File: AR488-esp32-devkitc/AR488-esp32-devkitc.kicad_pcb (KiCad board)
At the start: 2 copper layers, 63.5 x 50 mm, 7 parts, among them J2 Conn_02x12_Odd_Even, U2 ESP32-DevKitC

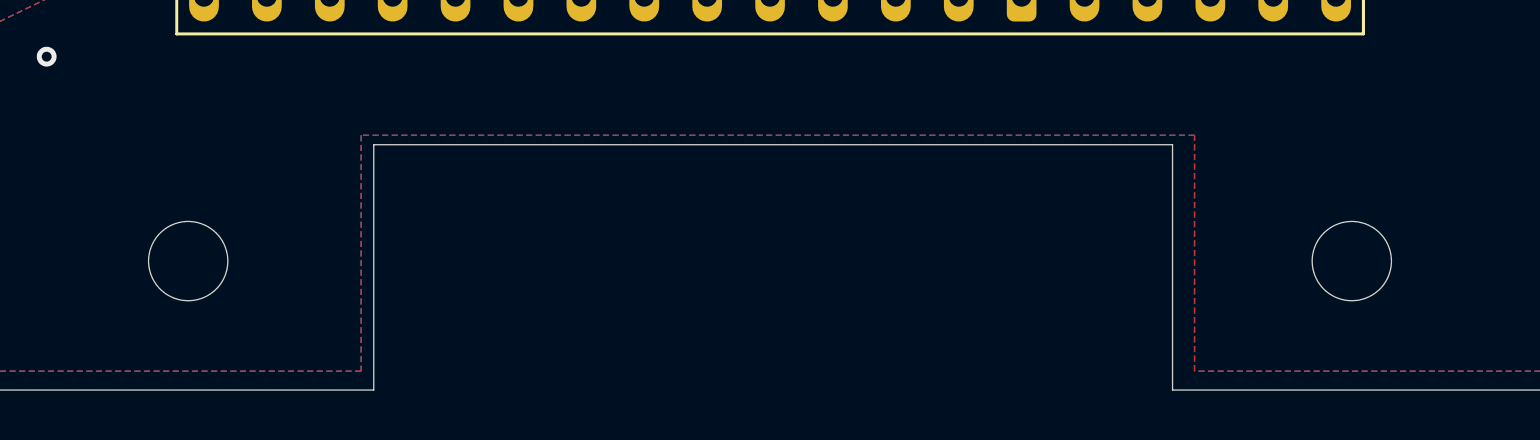
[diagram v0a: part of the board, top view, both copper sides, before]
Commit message: Several minor fixes and adjustments in PCBs
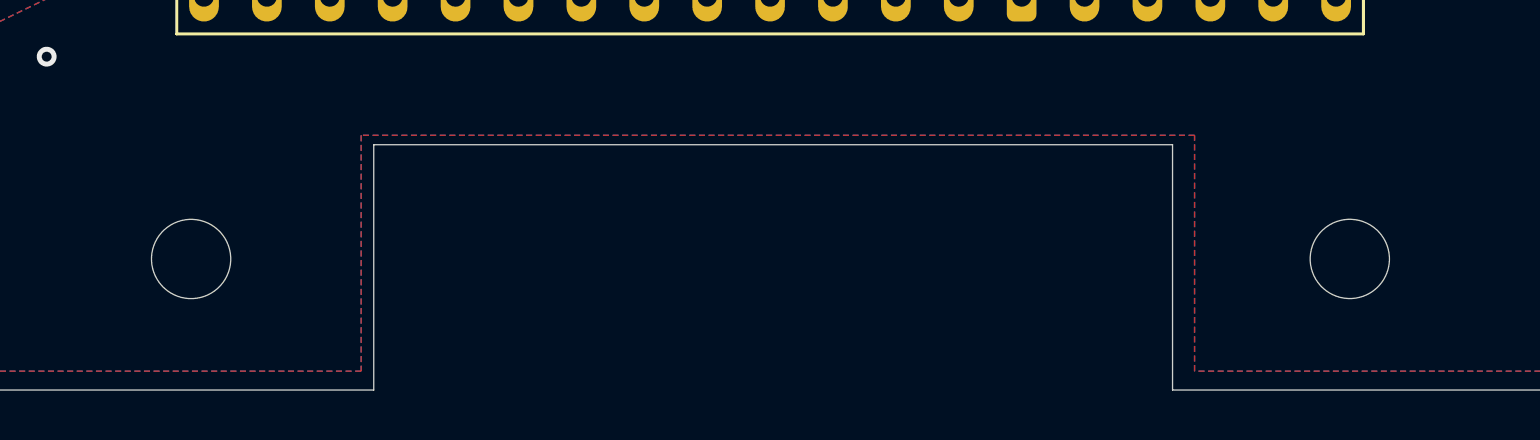
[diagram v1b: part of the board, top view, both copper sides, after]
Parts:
- moved REF** 0.15 mm to (71.4, 108.2)
- moved REF** 0.12 mm to (118.2, 108.2)
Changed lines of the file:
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@@
   (general
     (thickness 1.6)
-    (drawings 107)
+    (drawings 108)
     (tracks 100)
     (zones 0)
@@
       (outputformat 1)
       (mirror false)
-      (drillshape 1)
+      (drillshape 0)
       (scaleselection 1)
       (outputdirectory ""))
@@
   )
   (module MountingHole:MountingHole_3.2mm_M3_ISO7380 (layer F.Cu)
-    (at 118.245 108.325)
+    (at 118.164336 108.237955)
     (descr "Mounting Hole 3.2mm, no annular, M3, ISO7380")
     (tags "mounting hole 3.2mm no annular m3 iso7380")
@@
   )
   (module MountingHole:MountingHole_3.2mm_M3_ISO7380 (layer F.Cu)
-    (at 71.255 108.325)
+    (at 71.372767 108.240114)
     (descr "Mounting Hole 3.2mm, no annular, M3, ISO7380")
     (tags "mounting hole 3.2mm no annular m3 iso7380")
@@
     )
   )
+  (dimension 4.445 (width 0.15) (layer Dwgs.User)
+    (gr_text "4.445 mm" (at 65.2225 58.13) (layer Dwgs.User)
+      (effects (font (size 1 1) (thickness 0.15)))
+    )
+    (feature1 (pts (xy 63 67.685) (xy 63 58.843579)))
+    (feature2 (pts (xy 67.445 67.685) (xy 67.445 58.843579)))
+    (crossbar (pts (xy 67.445 59.43) (xy 63 59.43)))
+    (arrow1a (pts (xy 63 59.43) (xy 64.126504 58.843579)))
+    (arrow1b (pts (xy 63 59.43) (xy 64.126504 60.016421)))
+    (arrow2a (pts (xy 67.445 59.43) (xy 66.318496 58.843579)))
+    (arrow2b (pts (xy 67.445 59.43) (xy 66.318496 60.016421)))
+  )
   (gr_text http://whatever.sdfa3.org/gpib (at 98.56 75.305) (layer B.SilkS)

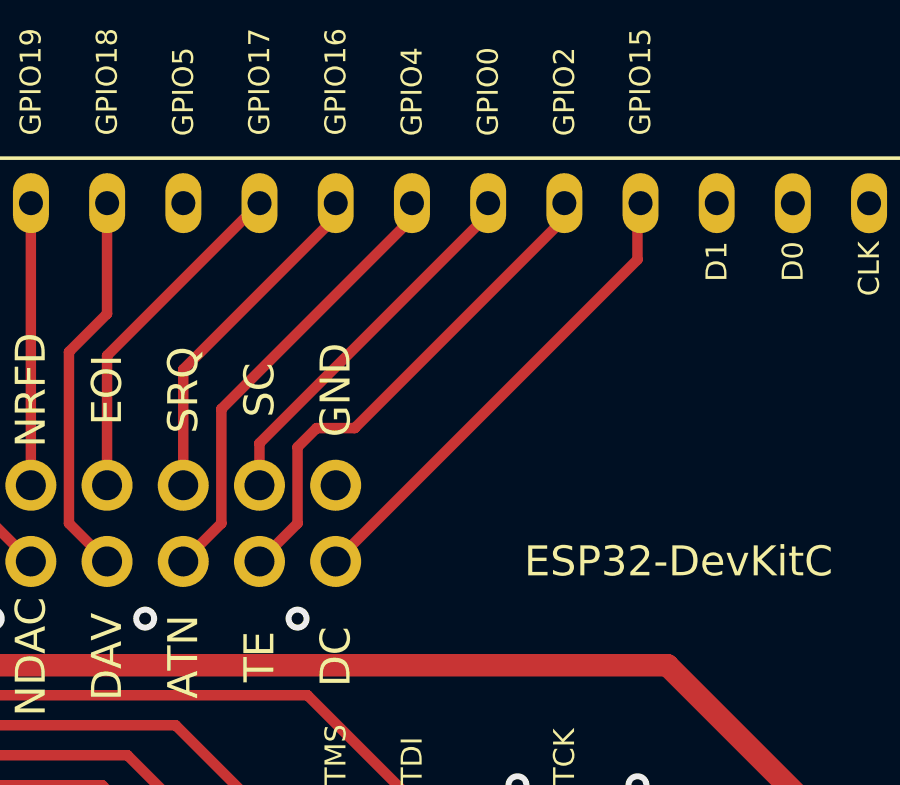
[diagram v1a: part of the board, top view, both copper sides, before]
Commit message: Fix the ESP32-devkitc board
- CMD was connected to GND
- swap GPIO2 dn GPIO15 to fix boot issues
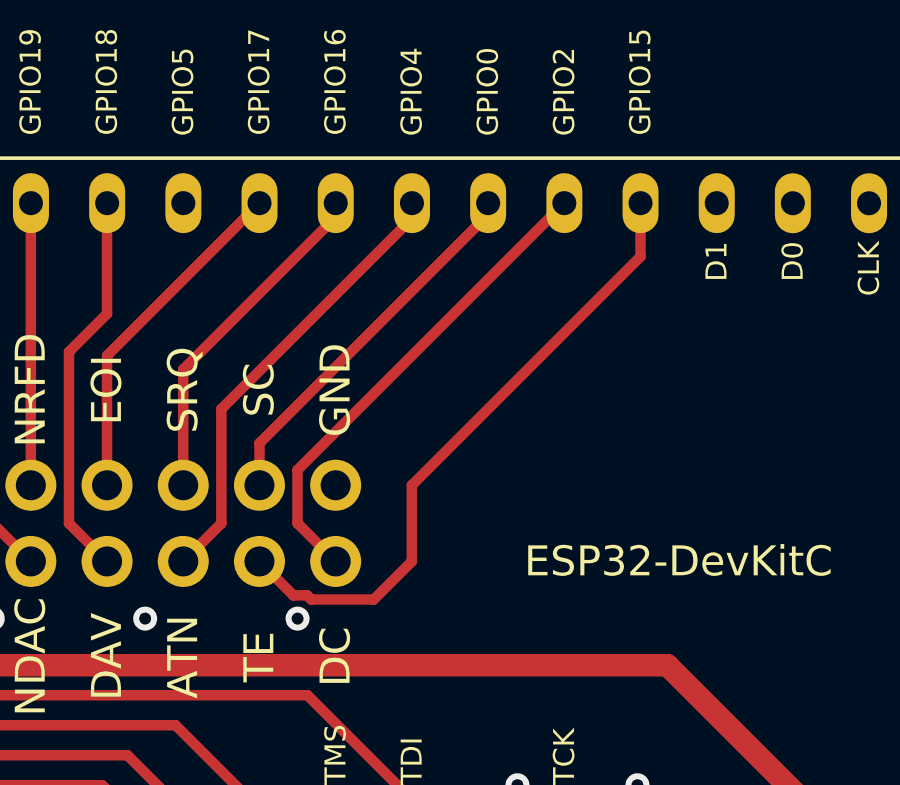
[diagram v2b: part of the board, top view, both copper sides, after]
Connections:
- U2 pad 1: Net-(U2-Pad1) -> unconnected-(U2-Pad1)
- U2 pad 16: Net-(U2-Pad16) -> unconnected-(U2-Pad16)
- U2 pad 17: Net-(U2-Pad17) -> unconnected-(U2-Pad17)
- U2 pad 18: GND -> unconnected-(U2-Pad18)
- U2 pad 2: Net-(U2-Pad2) -> unconnected-(U2-Pad2)
- U2 pad 20: Net-(U2-Pad20) -> unconnected-(U2-Pad20)
- U2 pad 21: Net-(U2-Pad21) -> unconnected-(U2-Pad21)
- U2 pad 22: Net-(U2-Pad22) -> unconnected-(U2-Pad22)
- U2 pad 23: DC -> TE
- U2 pad 24: TE -> DC
- U2 pad 29: Net-(U2-Pad29) -> unconnected-(U2-Pad29)
- U2 pad 3: Net-(U2-Pad3) -> unconnected-(U2-Pad3)
- U2 pad 34: Net-(U2-Pad34) -> unconnected-(U2-Pad34)
- U2 pad 35: Net-(U2-Pad35) -> unconnected-(U2-Pad35)
- U2 pad 4: Net-(U2-Pad4) -> unconnected-(U2-Pad4)
- U2 pad 5: Net-(U2-Pad5) -> unconnected-(U2-Pad5)
- U2 pad 6: Net-(U2-Pad6) -> unconnected-(U2-Pad6)
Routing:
- net TE: track 17.0 -> 21.2 mm
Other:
- net class Default removed
